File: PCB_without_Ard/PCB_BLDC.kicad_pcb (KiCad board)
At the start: 2 copper layers, 158.8 x 92.7 mm, 72 parts, among them J1 Ground Terminal, J2 Conn_01x03, J3 Conn_01x05, J4 Conn_01x02, J5 Conn_01x04, J6 Conn_01x04, J7 Conn_01x04, J8 Power Terminal, J9 Conn_01x02, Q1 IRF4905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

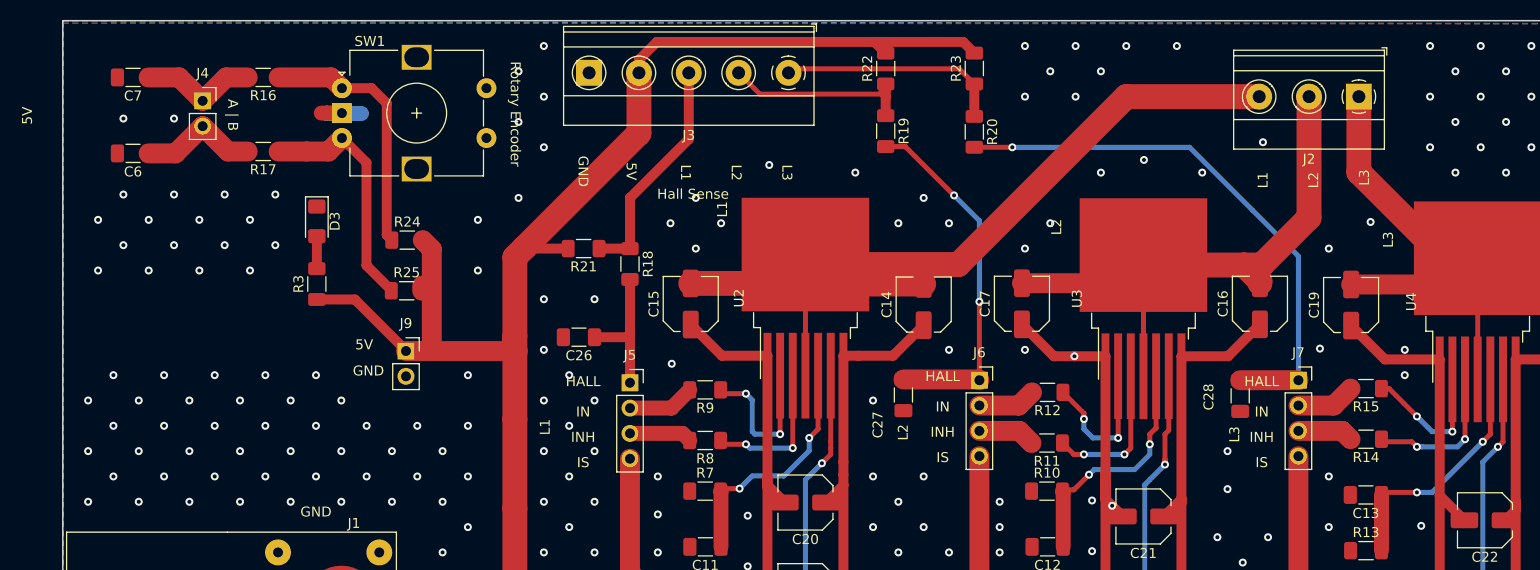
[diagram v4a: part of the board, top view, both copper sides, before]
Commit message: Add Push Button to Reset the System
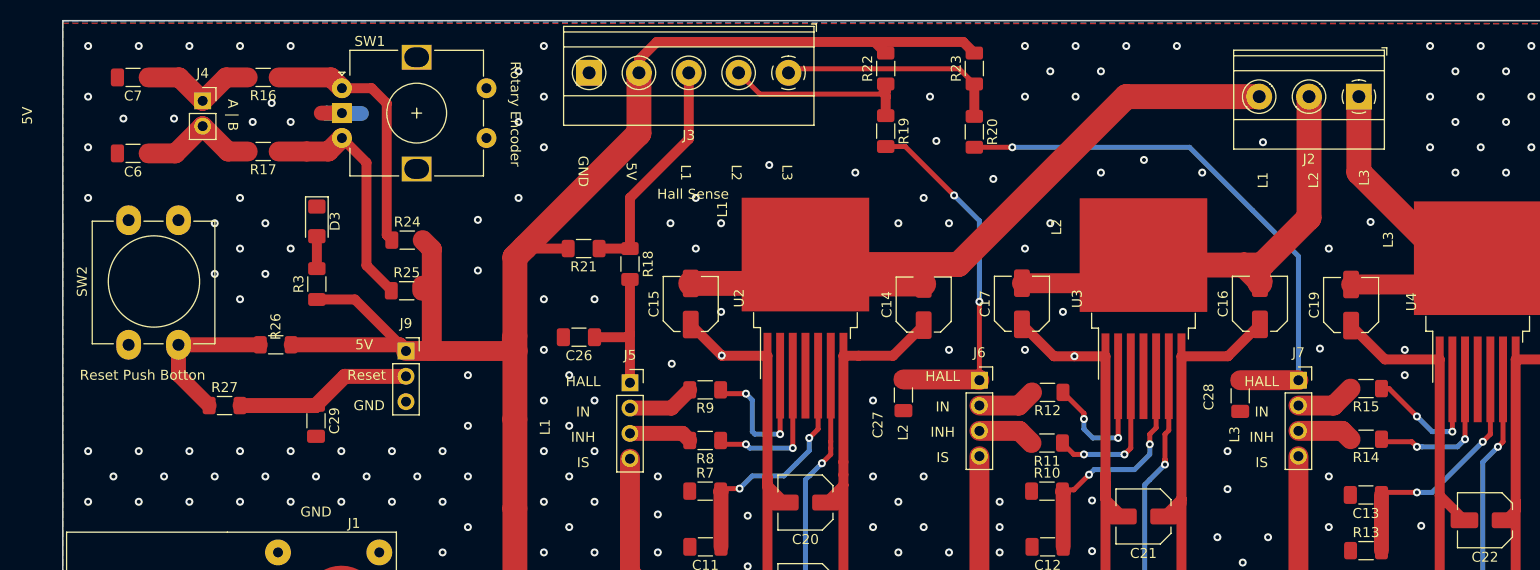
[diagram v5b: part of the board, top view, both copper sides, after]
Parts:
- added C29: 1uF, Capacitor_SMD:C_1206_3216Metric_Pad1.33x1.80mm_HandSolder, F.Cu at (66.0, 101.1)
- added R26: 10k, Resistor_SMD:R_1206_3216Metric_Pad1.30x1.75mm_HandSolder, F.Cu at (62.0, 93.5)
- added R27: 10k, Resistor_SMD:R_1206_3216Metric_Pad1.30x1.75mm_HandSolder, F.Cu at (56.9, 99.6)
- added SW2: SW_Push, Button_Switch_THT:SW_PUSH-12mm_Wuerth-430476085716, F.Cu at (47.2, 93.5)
- J9: footprint Connector_PinSocket_2.54mm:PinSocket_1x02_P2.54mm_Vertical -> Connector_PinSocket_2.54mm:PinSocket_1x03_P2.54mm_Vertical
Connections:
- J1 pad 2: GND -> (no net)
- J8 pad 2: GND -> (no net)
- J9 pad 2: GND -> /Reset_SW
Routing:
- net /Reset_SW: track 0.00 -> 17.9 mm
- net Net-(R26-Pad1): track 0.00 -> 15.6 mm
- net /VCC_5V: track 147.8 -> 159.6 mm
- net /L2_Motor: track 60.2 -> 51.1 mm
- net /L1_Motor: track 91.4 -> 82.3 mm
- net /L3_Motor: track 70.6 -> 61.6 mm
- net GND: vias 251 -> 241
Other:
- board text added: "Reset"
- board text added: "Reset Push Botton"

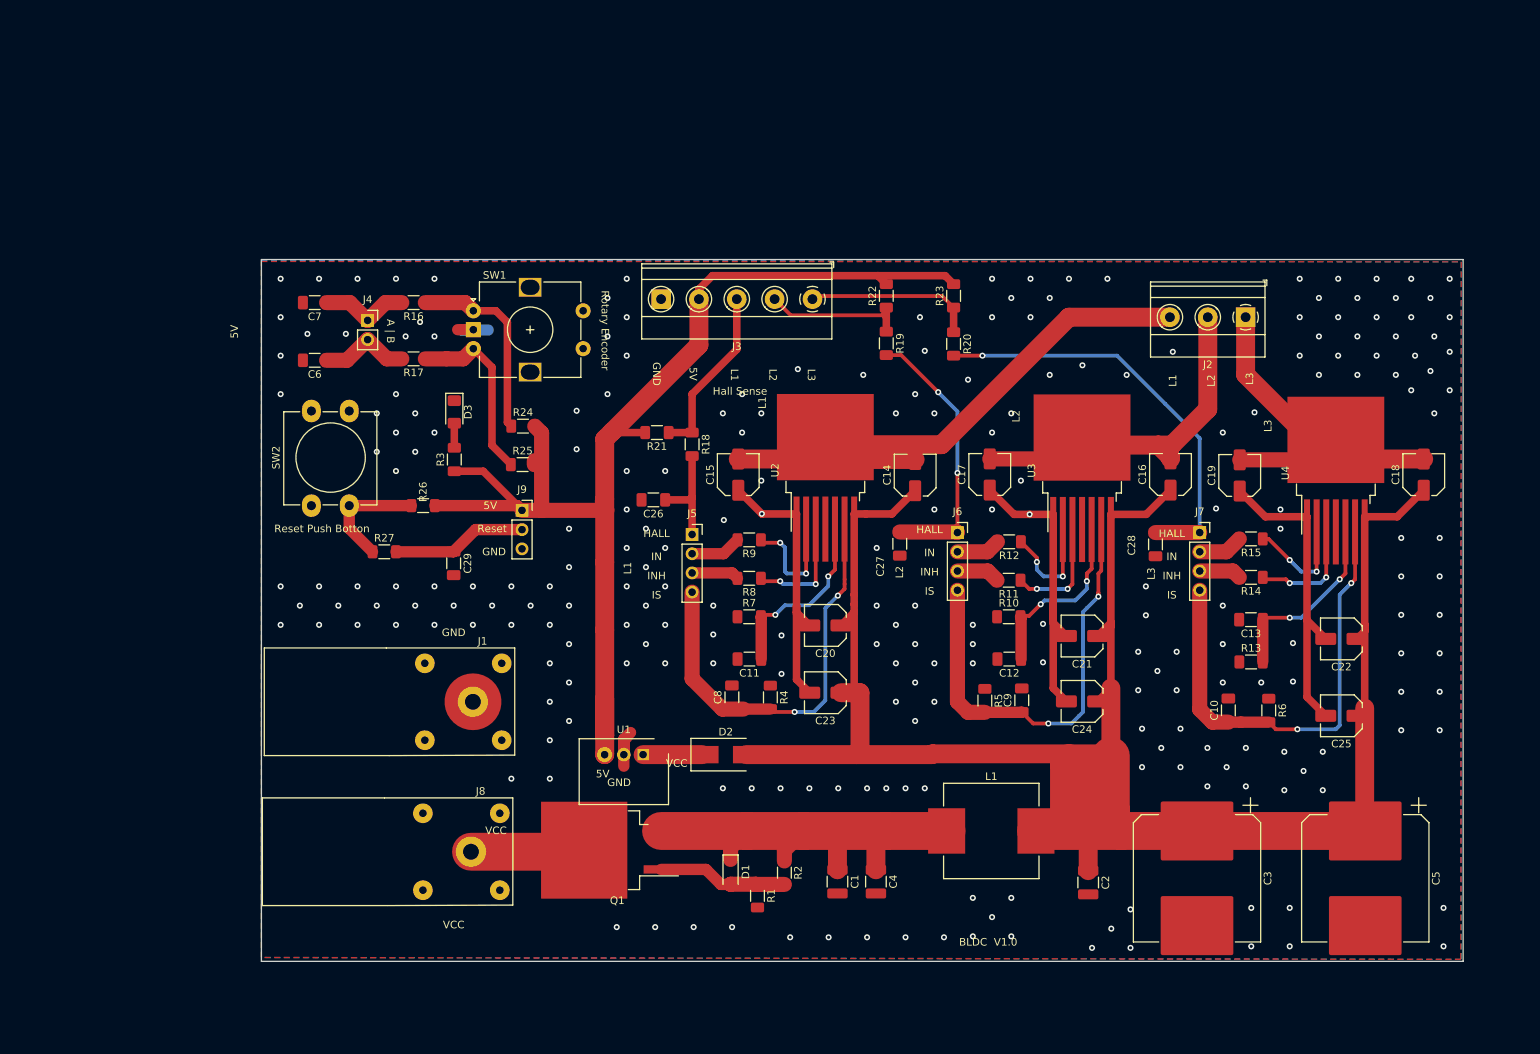
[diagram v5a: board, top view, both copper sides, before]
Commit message: PCB: Change Position of RC Filt for Hall Sense and Position of Connector
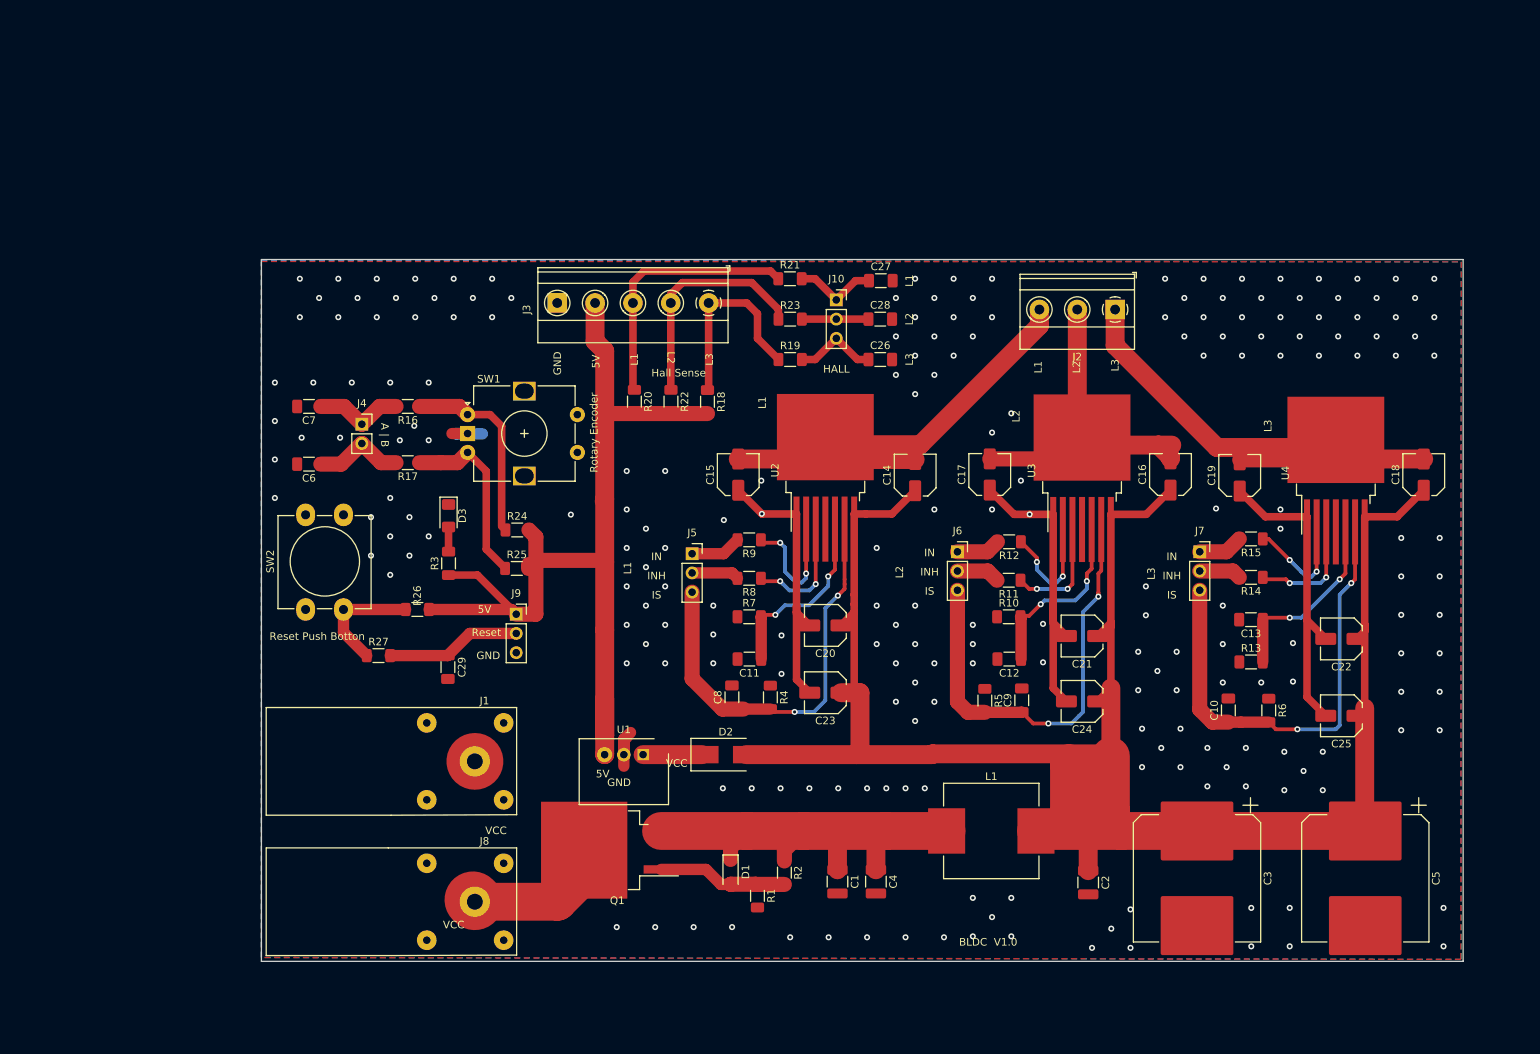
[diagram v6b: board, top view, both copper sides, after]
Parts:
- added J10: Conn_01x02, Connector_PinSocket_2.54mm:PinSocket_1x03_P2.54mm_Vertical, F.Cu at (116.6, 66.3)
- J5, J6, J7: value Conn_01x04 -> Conn_01x03; footprint Connector_PinSocket_2.54mm:PinSocket_1x04_P2.54mm_Vertical -> Connector_PinSocket_2.54mm:PinSocket_1x03_P2.54mm_Vertical
- moved C28 47.0 mm to (122.4, 68.8), turned to 0 degrees
- moved R20 42.8 mm to (89.9, 79.7)
- moved C26 35.2 mm to (122.4, 74.2), turned to 0 degrees
- moved C27 34.8 mm to (122.5, 63.8), turned to 0 degrees
- moved R22 31.7 mm to (94.7, 79.7), turned to 270 degrees
- moved R21 26.9 mm to (110.5, 63.5), turned to 0 degrees
- moved R23 21.8 mm to (110.5, 68.8), turned to 0 degrees
- moved J2 17.3 mm to (153.4, 67.6)
- moved C29 13.7 mm to (65.3, 114.8)
- moved C6 13.7 mm to (46.9, 88.0)
- moved J4 13.7 mm to (53.9, 82.7)
- moved R17 13.7 mm to (60.0, 87.8)
- moved R24 13.7 mm to (74.4, 96.7)
- moved R26 13.7 mm to (61.2, 107.2)
- moved R27 13.7 mm to (56.1, 113.3)
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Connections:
- C26 pad 1: Net-(C26-Pad1) -> /L3_Sense_Filt
- C27 pad 1: Net-(C27-Pad1) -> /L1_Sense_Filt
- C28 pad 1: Net-(C28-Pad1) -> /L2_Sense_Filt
- J5 pad 1: Net-(C26-Pad1) -> /L1_IN
- J5 pad 2: /L1_IN -> /L1_INH
- J5 pad 3: /L1_INH -> /L1_IS
- J6 pad 1: Net-(C27-Pad1) -> /L2_IN
- J6 pad 2: /L2_IN -> /L2_INH
- J6 pad 3: /L2_INH -> /L2_IS
- J7 pad 1: Net-(C28-Pad1) -> /L3_IN
- J7 pad 2: /L3_IN -> /L3_INH
- J7 pad 3: /L3_INH -> /L3_IS
- R18 pad 1: /L1_Sense -> /L3_Sense
- R18 pad 2: Net-(C26-Pad1) -> /VCC_5V
- R19 pad 1: /L2_Sense -> /L3_Sense
- R19 pad 2: Net-(C27-Pad1) -> /L3_Sense_Filt
- R20 pad 1: /L3_Sense -> /L1_Sense
- R20 pad 2: Net-(C28-Pad1) -> /VCC_5V
- R21 pad 2: /VCC_5V -> /L1_Sense_Filt
- R23 pad 1: /L3_Sense -> /L2_Sense
- R23 pad 2: /VCC_5V -> /L2_Sense_Filt
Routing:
- net Net-(C28-Pad1): track 55.3 -> 0.00 mm, vias 1 -> 0
- net Net-(C27-Pad1): track 36.1 -> 0.00 mm, vias 2 -> 0
- net /VCC_5V: track 159.6 -> 125.6 mm
- net /L3_Motor: track 61.6 -> 77.6 mm
- net /L1_Motor: track 82.3 -> 68.2 mm
- net Net-(C26-Pad1): track 14.0 -> 0.00 mm
- net /L1_Sense: track 23.2 -> 34.5 mm
- net /L3_Sense_Filt: track 0.00 -> 11.1 mm
- net /L1_Sense_Filt: track 0.00 -> 11.1 mm
- net /L2_Sense: track 19.3 -> 30.3 mm
- net /L2_Sense_Filt: track 0.00 -> 8.79 mm
- net /VCC_Unregulated: track 16.0 -> 20.2 mm
- net /L3_Sense: track 22.6 -> 25.8 mm
- net Net-(R9-Pad1): track 17.5 -> 18.9 mm
- net Net-(R8-Pad1): track 16.8 -> 17.5 mm
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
